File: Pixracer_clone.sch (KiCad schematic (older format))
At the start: 1 part

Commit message: finish schematic
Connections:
- net labels added: I2C2_SCl, I2C2_SDA, UART6_RX, UART6_TX
- net labels removed: SBUS, UART4_RX, UART4_TX
- wire segments 84 -> 89
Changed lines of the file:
@@
 Text GLabel 1150 3100 0    50   Input ~ 0
 OSC1-
-Text GLabel 3150 3900 2    50   Input ~ 0
+Text GLabel 3150 2500 2    50   Input ~ 0
 UART1_TX
-Text GLabel 3150 4000 2    50   Input ~ 0
+Text GLabel 3150 2600 2    50   Input ~ 0
 UART1_RX
 Text GLabel 3100 3000 2    50   Input ~ 0
@@
 Text GLabel 1200 6200 0    50   Input ~ 0
 TIM3_CH1
-Text GLabel 4350 3950 0    50   Input ~ 0
+Text GLabel 3200 5200 2    50   Input ~ 0
 LED1
-Text GLabel 4350 4150 0    50   Input ~ 0
+Text GLabel 3200 5000 2    50   Input ~ 0
 LED2
-Text GLabel 4350 4050 0    50   Input ~ 0
+Text GLabel 3200 5100 2    50   Input ~ 0
 LED3
-Text GLabel 4650 2850 0    50   Input ~ 0
-UART4_TX
-Text GLabel 4650 2950 0    50   Input ~ 0
-UART4_RX
 Text GLabel 1200 2000 0    50   Input ~ 0
 VCAP_1
@@
 Wire Wire Line
 	2200 6800 2200 7150
-Text GLabel 4150 2950 0    50   Input ~ 0
-SBUS
-Text GLabel 3150 3600 2    50   Input ~ 0
-SPI3_SCK
-Text GLabel 3150 3700 2    50   Input ~ 0
+Text GLabel 3700 3850 2    50   Input ~ 0
 SPI3_MISO
-Text GLabel 3150 3800 2    50   Input ~ 0
+Text GLabel 3700 3950 2    50   Input ~ 0
 SPI3_MOSI
-Wire Wire Line
-	4650 2950 4150 2950
-Wire Notes Line
-	750  700  3400 700
 Wire Notes Line
 	11150 1850 11150 650
 Wire Wire Line
-	4450 3950 4350 3950
+	3100 5200 3200 5200
 NoConn ~ 1700 1400
 Wire Wire Line
@@
 BATT_VOLT_SENSE
 Wire Wire Line
-	4350 4150 4450 4150
-Wire Wire Line
-	4350 4050 4450 4050
-Text GLabel 3250 5700 2    50   Input ~ 0
+	3200 5000 3100 5000
+Wire Wire Line
+	3200 5100 3100 5100
+Text GLabel 1150 6100 0    50   Input ~ 0
 SD_CS
 Text GLabel 3250 6000 2    50   Input ~ 0
@@
 	1300 6500 1200 6500
 Wire Wire Line
-	3100 5700 3250 5700
+	1300 6100 1150 6100
 Text GLabel 3250 4500 2    50   Input ~ 0
 EXTERNAL_MEM_CS
 Wire Wire Line
 	3100 4500 3250 4500
+Text GLabel 3700 3750 2    50   Input ~ 0
+SPI3_SCK
+Wire Wire Line
+	3100 2500 3150 2500
+Wire Wire Line
+	3100 2600 3150 2600
+Text GLabel 3250 5600 2    50   Input ~ 0
+UART6_TX
+Text GLabel 3250 5700 2    50   Input ~ 0
+UART6_RX
+Wire Wire Line
+	3100 5600 3250 5600
+Wire Wire Line
+	3100 5700 3250 5700
+Text GLabel 3250 4400 2    50   Input ~ 0
+I2C2_SDA
+Text GLabel 3250 4300 2    50   Input ~ 0
+I2C2_SCl
+Wire Wire Line
+	3100 4300 3250 4300
+Wire Wire Line
+	3100 4400 3250 4400
 $EndSCHEMATC

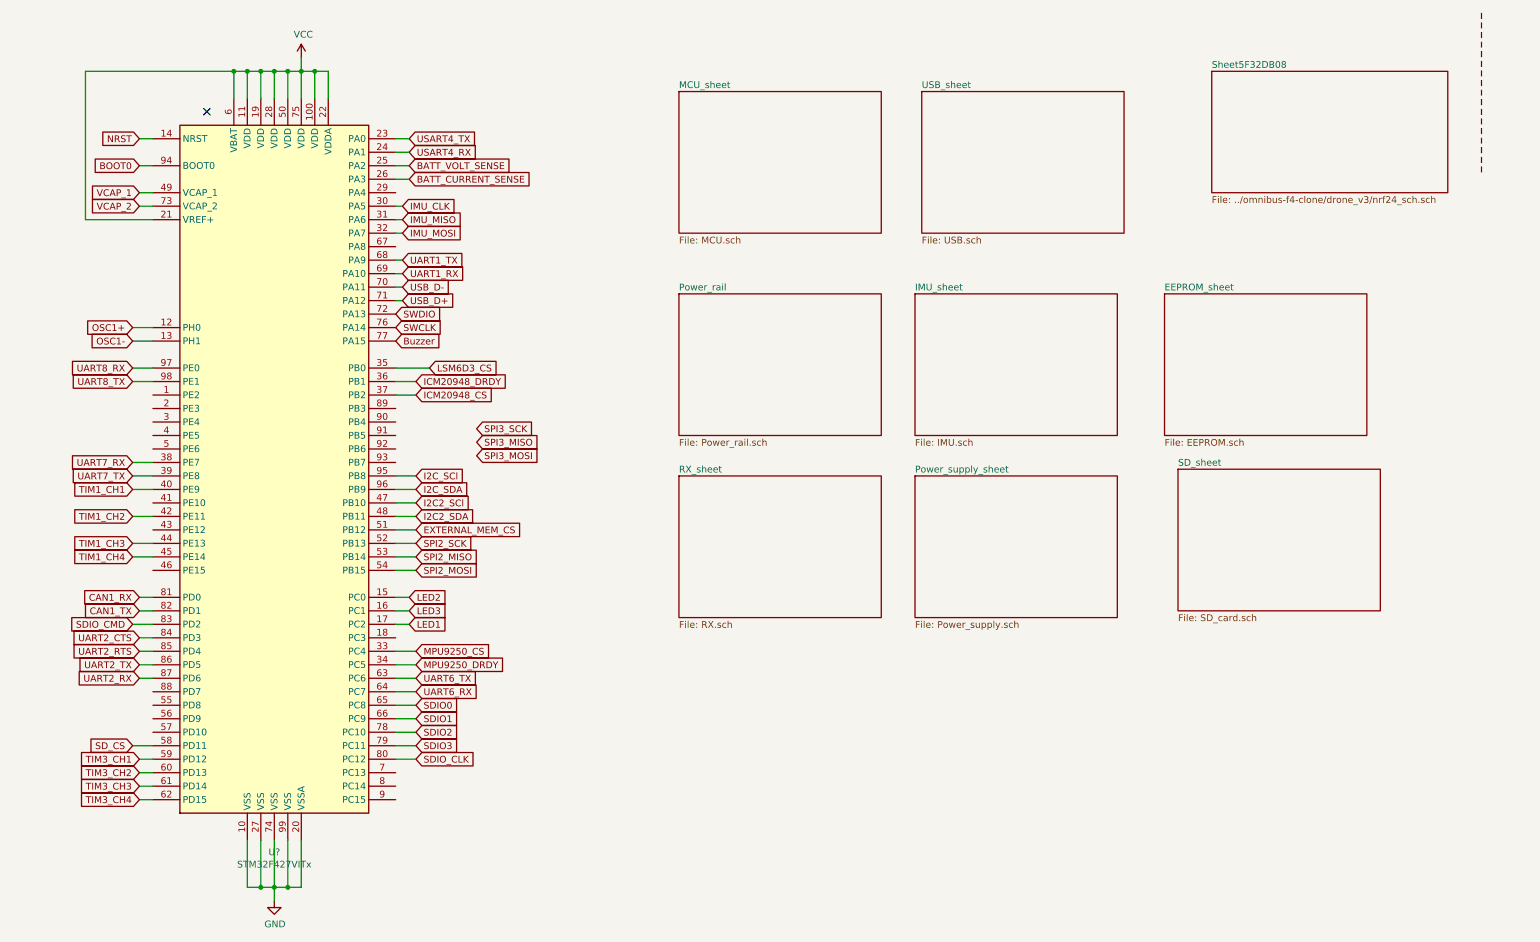
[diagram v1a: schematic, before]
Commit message: 4 layer add
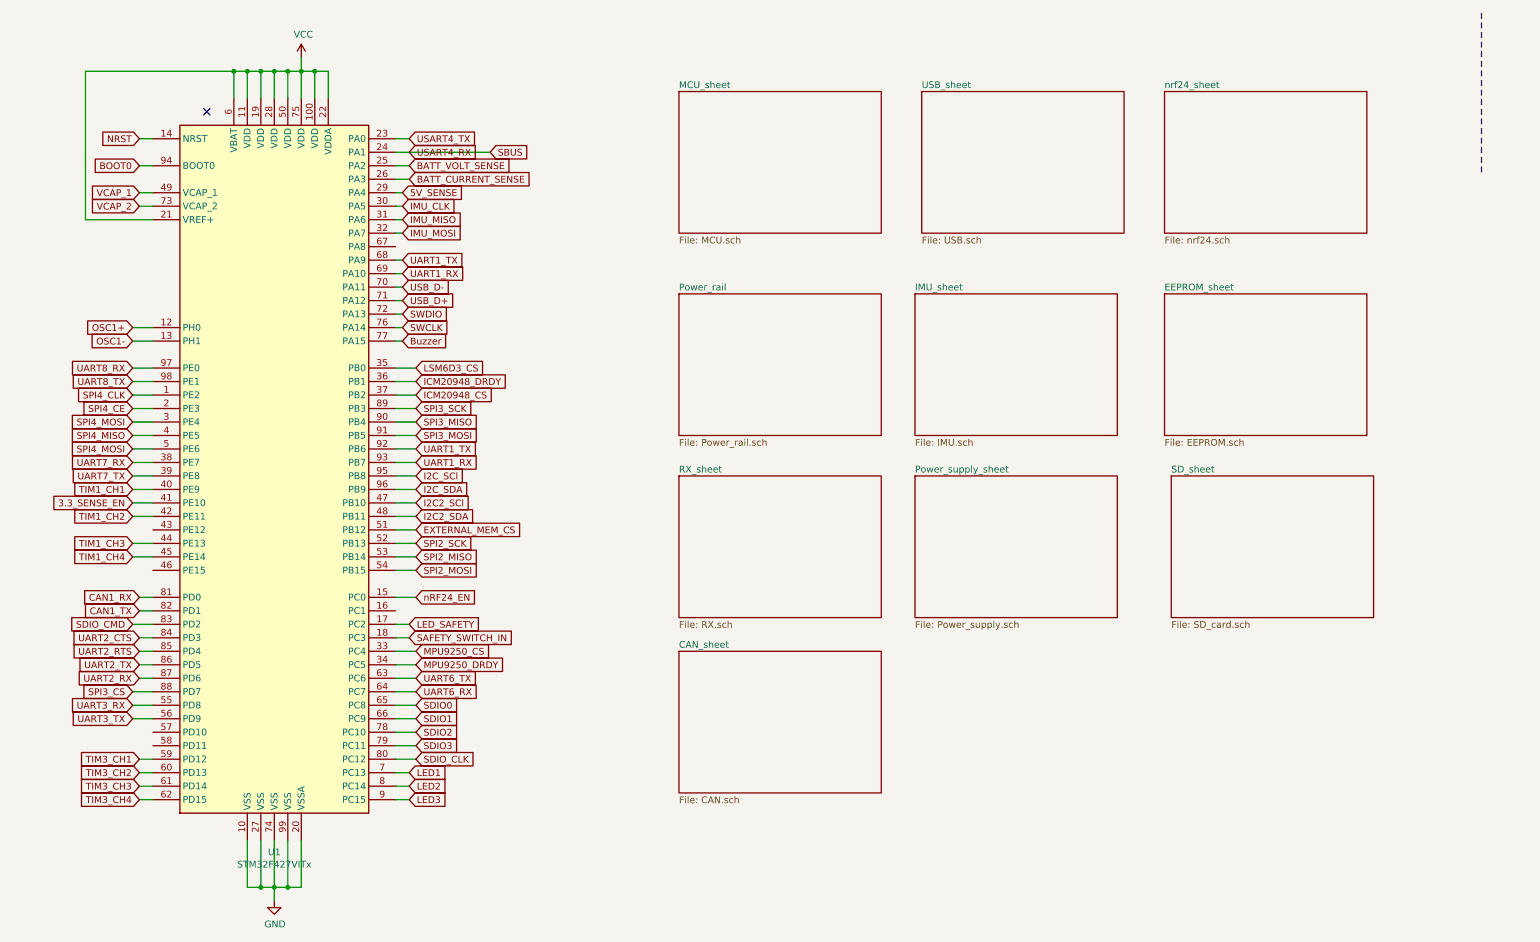
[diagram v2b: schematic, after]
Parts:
- gave numbers to parts that had none: 1
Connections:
- net LED1: now also U1.7 (PC13); no longer U1.17 (PC2)
- net LED2: now also U1.8 (PC14); no longer U1.15 (PC0)
- net LED3: now also U1.9 (PC15); no longer U1.16 (PC1)
- net SPI3_MISO: now also U1.90 (PB4)
- net SPI3_MOSI: now also U1.91 (PB5)
- net SPI3_SCK: now also U1.89 (PB3)
- net UART1_RX: now also U1.93 (PB7)
- net UART1_TX: now also U1.92 (PB6)
- net SPI4_CLK: now reaches U1.1 (PE2)
- net SAFETY_SWITCH_IN: now reaches U1.18 (PC3)
- net SPI4_CE: now reaches U1.2 (PE3)
- net 5V_SENSE: now reaches U1.29 (PA4)
- net SPI4_MOSI: now reaches U1.3 (PE4)
- net SPI4_MOSI: now also U1.5 (PE6)
- net SPI4_MISO: now reaches U1.4 (PE5)
- net 3.3_SENSE_EN: now reaches U1.41 (PE10)
- net UART3_RX: now reaches U1.55 (PD8)
- net UART3_TX: now reaches U1.56 (PD9)
- net SPI3_CS: now reaches U1.88 (PD7)
- net SD_CS: no longer names the net of U1.58 (PD11)
- net USART4_RX renamed SBUS
- new net LED_SAFETY: U1.17 (PC2)
- new net nRF24_EN: U1.15 (PC0)
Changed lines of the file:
@@
 $Descr A4 11693 8268
 encoding utf-8
-Sheet 1 10
+Sheet 1 11
 Title ""
 Date ""
@@
 Text GLabel 3150 2600 2    50   Input ~ 0
 UART1_RX
-Text GLabel 3100 3000 2    50   Input ~ 0
+Text GLabel 3150 3000 2    50   Input ~ 0
 SWCLK
-Text GLabel 3100 2900 2    50   Input ~ 0
+Text GLabel 3150 2900 2    50   Input ~ 0
 SWDIO
 Text GLabel 3250 4200 2    50   Input ~ 0
@@
 Text GLabel 1200 6200 0    50   Input ~ 0
 TIM3_CH1
-Text GLabel 3200 5200 2    50   Input ~ 0
+Text GLabel 3200 6300 2    50   Input ~ 0
 LED1
-Text GLabel 3200 5000 2    50   Input ~ 0
+Text GLabel 3200 6400 2    50   Input ~ 0
 LED2
-Text GLabel 3200 5100 2    50   Input ~ 0
+Text GLabel 3200 6500 2    50   Input ~ 0
 LED3
 Text GLabel 1200 2000 0    50   Input ~ 0
@@
 Wire Wire Line
 	2200 6800 2200 7150
-Text GLabel 3700 3850 2    50   Input ~ 0
+Text GLabel 3250 3700 2    50   Input ~ 0
 SPI3_MISO
-Text GLabel 3700 3950 2    50   Input ~ 0
+Text GLabel 3250 3800 2    50   Input ~ 0
 SPI3_MOSI
 Wire Notes Line
 	11150 1850 11150 650
 Wire Wire Line
-	3100 5200 3200 5200
+	3100 6300 3200 6300
 NoConn ~ 1700 1400
 Wire Wire Line
@@
 BATT_VOLT_SENSE
 Wire Wire Line
-	3200 5000 3100 5000
-Wire Wire Line
-	3200 5100 3100 5100
-Text GLabel 1150 6100 0    50   Input ~ 0
-SD_CS
+	3200 6400 3100 6400
+Wire Wire Line
+	3200 6500 3100 6500
 Text GLabel 3250 6000 2    50   Input ~ 0
 SDIO2
@@
 Text GLabel 3150 2800 2    50   Input ~ 0
 USB_D+
-$Sheet
-S 9150 1100 1750 900
-U 5F32DB09
-F0 "Sheet5F32DB08" 50
-F1 "../omnibus-f4-clone/drone_v3/nrf24_sch.sch" 50
-$EndSheet
 Wire Wire Line
 	3100 4700 3250 4700
 Wire Wire Line
 	3250 4800 3100 4800
-Text GLabel 3100 3100 2    50   Input ~ 0
+Text GLabel 3150 3100 2    50   Input ~ 0
 Buzzer
 $Comp
-L MCU_ST_STM32F4:STM32F427VITx U?
+L MCU_ST_STM32F4:STM32F427VITx U1
 U 1 1 5F785842
 P 2200 4000
-F 0 "U?" H 2200 1111 50  0000 C CNN
+F 0 "U1" H 2200 1111 50  0000 C CNN
 F 1 "STM32F427VITx" H 2200 1020 50  0000 C CNN
 F 2 "Package_QFP:LQFP-100_14x14mm_P0.5mm" H 1500 1400 50  0001 R CNN
@@
 $EndSheet
 $Sheet
-S 8900 4050 1500 1050
+S 8850 4100 1500 1050
 U 5F6068B8
 F0 "SD_sheet" 50
@@
 Text GLabel 3250 3500 2    50   Input ~ 0
 ICM20948_CS
-Text GLabel 3350 3300 2    50   Input ~ 0
+Text GLabel 3250 3300 2    50   Input ~ 0
 LSM6D3_CS
-Wire Wire Line
-	3350 3300 3100 3300
 Text GLabel 3250 5500 2    50   Input ~ 0
 MPU9250_DRDY
@@
 	3100 1600 3200 1600
 Wire Wire Line
-	3200 1700 3100 1700
-Wire Wire Line
 	3100 4600 3250 4600
 Wire Wire Line
@@
 Wire Wire Line
 	1300 6500 1200 6500
-Wire Wire Line
-	1300 6100 1150 6100
 Text GLabel 3250 4500 2    50   Input ~ 0
 EXTERNAL_MEM_CS
 Wire Wire Line
 	3100 4500 3250 4500
-Text GLabel 3700 3750 2    50   Input ~ 0
+Text GLabel 3250 3600 2    50   Input ~ 0
 SPI3_SCK
 Wire Wire Line
@@
 Wire Wire Line
 	3100 4400 3250 4400
+Wire Wire Line
+	3100 2900 3150 2900
+Wire Wire Line
+	3100 3000 3150 3000
+Wire Wire Line
+	3150 3100 3100 3100
+$Sheet
+S 5200 5400 1500 1050
+U 5FC6E587
+F0 "CAN_sheet" 50
+F1 "CAN.sch" 50
+$EndSheet
+Text GLabel 1150 4300 0    50   Input ~ 0
+3.3_SENSE_EN
+Wire Wire Line
+	1150 4300 1300 4300
+Wire Wire Line
+	3100 3600 3250 3600
+Wire Wire Line
+	3100 3700 3250 3700
+Wire Wire Line
+	3100 3800 3250 3800
+Text GLabel 1150 5700 0    50   Input ~ 0
+SPI3_CS
+Wire Wire Line
+	1300 5700 1150 5700
+Text GLabel 1150 5900 0    50   Input ~ 0
+UART3_TX
+Text GLabel 1150 5800 0    50   Input ~ 0
+UART3_RX
+Wire Wire Line
+	1300 5900 1150 5900
+Wire Wire Line
+	1300 5800 1150 5800
+Text GLabel 3250 3900 2    50   Input ~ 0
+UART1_TX
+Text GLabel 3250 4000 2    50   Input ~ 0
+UART1_RX
+Wire Wire Line
+	3100 3900 3250 3900
+Wire Wire Line
+	3100 4000 3250 4000
+Wire Wire Line
+	3100 3300 3250 3300
+Text GLabel 3200 5300 2    50   Input ~ 0
+SAFETY_SWITCH_IN
+Wire Wire Line
+	3100 5300 3200 5300
+Text GLabel 3200 5200 2    50   Input ~ 0
+LED_SAFETY
+Wire Wire Line
+	3100 5200 3200 5200
+Text GLabel 3150 2000 2    50   Input ~ 0
+5V_SENSE
+Wire Wire Line
+	3100 2000 3150 2000
+$Sheet
+S 8800 1250 1500 1050
+U 5FD47887
+F0 "nrf24_sheet" 50
+F1 "nrf24.sch" 50
+$EndSheet
+Text GLabel 1150 3800 0    50   Input ~ 0
+SPI4_MISO
+Text GLabel 1150 3900 0    50   Input ~ 0
+SPI4_MOSI
+Text GLabel 1150 3500 0    50   Input ~ 0
+SPI4_CLK
+Wire Wire Line
+	1300 3500 1150 3500
+Wire Wire Line
+	1300 3800 1150 3800
+Wire Wire Line
+	1300 3900 1150 3900
+Text GLabel 1150 3600 0    50   Input ~ 0
+SPI4_CE
+Text GLabel 1150 3700 0    50   Input ~ 0
+SPI4_MOSI
+Wire Wire Line
+	1150 3600 1300 3600
+Wire Wire Line
+	1300 3700 1150 3700
+Text GLabel 3250 5000 2    50   Input ~ 0
+nRF24_EN
+Wire Wire Line
+	3250 5000 3100 5000
+Text GLabel 3800 1700 2    50   Input ~ 0
+SBUS
+Wire Wire Line
+	3100 1700 3800 1700
 $EndSCHEMATC

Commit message: add alot
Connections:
- net UART1_RX: no longer U1.69 (PA10)
- net UART1_TX: no longer U1.68 (PA9)
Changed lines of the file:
@@
 Text GLabel 1150 3100 0    50   Input ~ 0
 OSC1-
-Text GLabel 3150 2500 2    50   Input ~ 0
-UART1_TX
-Text GLabel 3150 2600 2    50   Input ~ 0
-UART1_RX
 Text GLabel 3150 3000 2    50   Input ~ 0
 SWCLK
@@
 Text GLabel 3250 3600 2    50   Input ~ 0
 SPI3_SCK
-Wire Wire Line
-	3100 2500 3150 2500
-Wire Wire Line
-	3100 2600 3150 2600
 Text GLabel 3250 5600 2    50   Input ~ 0
 UART6_TX

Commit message: a
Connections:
- net EXTERNAL_MEM_CS: now also U1.57 (PD10); no longer U1.51 (PB12)
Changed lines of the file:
@@
 Wire Wire Line
 	1300 6500 1200 6500
-Text GLabel 3250 4500 2    50   Input ~ 0
+Text GLabel 1150 6000 0    50   Input ~ 0
 EXTERNAL_MEM_CS
 Wire Wire Line
-	3100 4500 3250 4500
+	1300 6000 1150 6000
 Text GLabel 3250 3600 2    50   Input ~ 0
 SPI3_SCK

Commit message: finish board
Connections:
- net EXTERNAL_MEM_CS: now also U1.51 (PB12); no longer U1.57 (PD10)
- net SPI4_MOSI: no longer U1.3 (PE4)
- net EXTERNAL_MPU_CS: now reaches U1.43 (PE12)
- new net SPI4_CS: U1.3 (PE4)
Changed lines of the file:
@@
 Wire Wire Line
 	1300 6500 1200 6500
-Text GLabel 1150 6000 0    50   Input ~ 0
+Text GLabel 3250 4500 2    50   Input ~ 0
 EXTERNAL_MEM_CS
 Wire Wire Line
-	1300 6000 1150 6000
+	3100 4500 3250 4500
 Text GLabel 3250 3600 2    50   Input ~ 0
 SPI3_SCK
@@
 SPI4_CE
 Text GLabel 1150 3700 0    50   Input ~ 0
-SPI4_MOSI
+SPI4_CS
 Wire Wire Line
 	1150 3600 1300 3600
@@
 Wire Wire Line
 	3100 1700 3800 1700
+Text GLabel 1150 4500 0    50   Input ~ 0
+EXTERNAL_MPU_CS
+Wire Wire Line
+	1150 4500 1300 4500
 $EndSCHEMATC
